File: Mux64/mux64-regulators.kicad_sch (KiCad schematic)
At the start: 23 parts

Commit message: Add files via upload
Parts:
- C1, C2, C3, C4, C7: renamed from C?; footprint (none) -> Capacitor_SMD:C_0805_2012Metric
- C10, C11, C12, C5, C6, C8, C9: renamed from C?; footprint (none) -> Capacitor_SMD:C_0201_0603Metric
- gave numbers to parts that had none: 11

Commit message: Add files via upload
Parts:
- J10, J7, J8, J9: footprint (none) -> Connector_PinSocket_1.00mm:PinSocket_2x10_P1.00mm_Vertical_SMD
- R4, R5, R6, R7: footprint (none) -> Resistor_SMD:R_0603_1608Metric
- TP1: footprint (none) -> TestPoint:TestPoint_Pad_D2.5mm
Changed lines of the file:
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@@
       (effects (font (size 0.75 0.75)))
     )
-    (property "Footprint" "" (id 2) (at 121.92 134.62 0)
+    (property "Footprint" "Resistor_SMD:R_0603_1608Metric" (id 2) (at 121.92 134.62 0)
       (effects (font (size 1.27 1.27)) hide)
     )
@@
     (property "Reference" "J7" (id 0) (at 29.21 34.29 0))
     (property "Value" "Conn_01x20" (id 1) (at 29.21 29.21 0))
-    (property "Footprint" "" (id 2) (at 29.21 55.88 0)
+    (property "Footprint" "Connector_PinSocket_1.00mm:PinSocket_2x10_P1.00mm_Vertical_SMD" (id 2) (at 29.21 55.88 0)
       (effects (font (size 1.27 1.27)) hide)
     )
@@
       (effects (font (size 0.75 0.75)))
     )
-    (property "Footprint" "" (id 2) (at 121.92 116.84 0)
+    (property "Footprint" "Resistor_SMD:R_0603_1608Metric" (id 2) (at 121.92 116.84 0)
       (effects (font (size 1.27 1.27)) hide)
     )
@@
       (effects (font (size 0.75 0.75)))
     )
-    (property "Footprint" "" (id 2) (at 125.73 106.68 0)
+    (property "Footprint" "TestPoint:TestPoint_Pad_D2.5mm" (id 2) (at 125.73 106.68 0)
       (effects (font (size 1.27 1.27)) hide)
     )
@@
     (property "Reference" "J10" (id 0) (at 99.06 34.29 0))
     (property "Value" "Conn_01x20" (id 1) (at 99.06 29.21 0))
-    (property "Footprint" "" (id 2) (at 99.06 55.88 0)
+    (property "Footprint" "Connector_PinSocket_1.00mm:PinSocket_2x10_P1.00mm_Vertical_SMD" (id 2) (at 99.06 55.88 0)
       (effects (font (size 1.27 1.27)) hide)
     )
@@
     (property "Reference" "J8" (id 0) (at 52.07 34.29 0))
     (property "Value" "Conn_01x20" (id 1) (at 52.07 29.21 0))
-    (property "Footprint" "" (id 2) (at 52.07 55.88 0)
+    (property "Footprint" "Connector_PinSocket_1.00mm:PinSocket_2x10_P1.00mm_Vertical_SMD" (id 2) (at 52.07 55.88 0)
       (effects (font (size 1.27 1.27)) hide)
     )
@@
       (effects (font (size 0.75 0.75)))
     )
-    (property "Footprint" "" (id 2) (at 121.92 140.97 0)
+    (property "Footprint" "Resistor_SMD:R_0603_1608Metric" (id 2) (at 121.92 140.97 0)
       (effects (font (size 1.27 1.27)) hide)
     )
@@
     (property "Reference" "J9" (id 0) (at 76.2 34.29 0))
     (property "Value" "Conn_01x20" (id 1) (at 76.2 29.21 0))
-    (property "Footprint" "" (id 2) (at 76.2 55.88 0)
+    (property "Footprint" "Connector_PinSocket_1.00mm:PinSocket_2x10_P1.00mm_Vertical_SMD" (id 2) (at 76.2 55.88 0)
       (effects (font (size 1.27 1.27)) hide)
     )
@@
       (effects (font (size 0.75 0.75)))
     )
-    (property "Footprint" "" (id 2) (at 129.54 116.84 0)
-      (effects (font (size 1.27 1.27)) hide)
-    )
+    (property "Footprint" "Resistor_SMD:R_0603_1608Metric" (id 2) (at 129.54 116.84 0)
+      (effects (font (size 1.27 1.27)) hide)
+    )

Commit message: Add files via upload
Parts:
- removed J10, J7, J8, J9: Conn_01x20, Connector_PinSocket_1.00mm:PinSocket_2x10_P1.00mm_Vertical_SMD, symbol Connector_Generic:Conn_01x20
- added J10, J7, J8, J9: Conn_01x24, Connector_PinSocket_2.54mm:PinSocket_2x12_P2.54mm_Vertical, symbol Connector_Generic:Conn_01x24
- added R8: 0ohm, Resistor_SMD:R_0805_2012Metric, symbol Device:R_Small_US
- C10, C11, C12, C5, C6, C8, C9: footprint Capacitor_SMD:C_0201_0603Metric -> Capacitor_SMD:C_0805_2012Metric
- R4, R5, R6, R7: footprint Resistor_SMD:R_0603_1608Metric -> Resistor_SMD:R_0805_2012Metric
- U1: footprint (none) -> Package_TO_SOT_SMD:SOT-223-3_TabPin2
- U2: footprint (none) -> Package_TO_SOT_SMD:SOT-23-6
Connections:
- net 1.2V: now also C10.1, C11.1, C12.1, C7.1, C9.1, J10.3 (Pin_3), J10.5 (Pin_5), J10.6 (Pin_6), J10.7 (Pin_7), J10.8 (Pin_8); no longer C10.2, C11.2, C12.2, C7.2, C9.2
- net B_a0(MUX_OUT): now also J10.14 (Pin_14)
- net B_a4: now also J10.13 (Pin_13)
- net B_d0: now also J7.8 (Pin_8)
- net B_d1: now also J7.5 (Pin_5)
- net B_d2: now also J7.6 (Pin_6)
- net B_d3: now also J7.3 (Pin_3)
- net B_d4: now also J7.4 (Pin_4)
- net B_d5: now also J7.2 (Pin_2)
- net GND: now also C10.2, C11.2, C12.2, C7.2, C9.2, J10.1 (Pin_1), J10.10 (Pin_10), J10.11 (Pin_11), J10.12 (Pin_12), J10.2 (Pin_2), J10.9 (Pin_9), J7.23 (Pin_23), J7.24 (Pin_24), J8.23 (Pin_23), J8.24 (Pin_24), J9.23 (Pin_23), J9.24 (Pin_24), R8.1; no longer C10.1, C11.1, C12.1, C7.1, C9.1
- net MUX64_A0: now also J10.15 (Pin_15), J10.16 (Pin_16), J10.17 (Pin_17), J7.10 (Pin_10), J7.7 (Pin_7), J8.15 (Pin_15), J8.2 (Pin_2), J9.11 (Pin_11), J9.13 (Pin_13), J9.15 (Pin_15), J9.17 (Pin_17), J9.19 (Pin_19), J9.2 (Pin_2), J9.3 (Pin_3), J9.9 (Pin_9), R8.2
- net MUX64_A10: now also J7.17 (Pin_17)
- net MUX64_A11: now also J7.20 (Pin_20)
- net MUX64_A12: now also J7.19 (Pin_19)
- net MUX64_A13: now also J7.22 (Pin_22)
- net MUX64_A15: now also J8.4 (Pin_4)
- net MUX64_A16: now also J8.3 (Pin_3)
- net MUX64_A17: now also J8.6 (Pin_6)
- net MUX64_A18: now also J8.5 (Pin_5)
- net MUX64_A19: now also J8.8 (Pin_8)
- net MUX64_A2: now also J7.9 (Pin_9)
- net MUX64_A20: now also J8.7 (Pin_7)
- net MUX64_A21: now also J8.10 (Pin_10)
- net MUX64_A22: now also J8.9 (Pin_9)
- net MUX64_A23: now also J8.12 (Pin_12)
- net MUX64_A24: now also J8.11 (Pin_11)
- net MUX64_A25: now also J8.14 (Pin_14)
- net MUX64_A26: now also J8.13 (Pin_13)
- net MUX64_A27: now also J8.16 (Pin_16)
- net MUX64_A29: now also J8.18 (Pin_18)
- net MUX64_A3: now also J7.12 (Pin_12)
- net MUX64_A30: now also J8.17 (Pin_17)
- net MUX64_A31: now also J8.20 (Pin_20)
- net MUX64_A32: now also J8.19 (Pin_19)
- net MUX64_A33: now also J8.22 (Pin_22)
- net MUX64_A35: now also J9.4 (Pin_4)
- net MUX64_A37: now also J9.6 (Pin_6)
- net MUX64_A38: now also J9.5 (Pin_5)
- net MUX64_A39: now also J9.8 (Pin_8)
- net MUX64_A4: now also J7.11 (Pin_11)
- net MUX64_A40: now also J9.7 (Pin_7)
- net MUX64_A41: now also J9.10 (Pin_10)
- net MUX64_A43: now also J9.12 (Pin_12)
- net MUX64_A45: now also J9.14 (Pin_14)
- net MUX64_A47: now also J9.16 (Pin_16)
- net MUX64_A49: now also J9.18 (Pin_18)
- net MUX64_A5: now also J7.14 (Pin_14)
- net MUX64_A51: now also J9.20 (Pin_20)
- net MUX64_A53: now also J9.22 (Pin_22)
- net MUX64_A54: now also J10.23 (Pin_23)
- net MUX64_A55: now also J10.21 (Pin_21)
- net MUX64_A56: now also J10.22 (Pin_22)
- net MUX64_A57: now also J10.19 (Pin_19)
- net MUX64_A58: now also J10.20 (Pin_20)
- net MUX64_A6: now also J7.13 (Pin_13)
- net MUX64_A60: now also J10.18 (Pin_18)
- net MUX64_A7: now also J7.16 (Pin_16)
- net MUX64_A8: now also J7.15 (Pin_15)
- net MUX64_A9: now also J7.18 (Pin_18)
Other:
- note added: "Unused Mux inputs"

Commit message: Add files via upload
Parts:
- removed R8: 0ohm, Resistor_SMD:R_0805_2012Metric, symbol Device:R_Small_US
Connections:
- net MUX64_A0 is gone; now on net GND: J10.15 (Pin_15), J10.16 (Pin_16), J10.17 (Pin_17), J7.10 (Pin_10), J7.7 (Pin_7), J8.15 (Pin_15), J8.2 (Pin_2), J9.11 (Pin_11), J9.13 (Pin_13), J9.15 (Pin_15), J9.17 (Pin_17), J9.19 (Pin_19), J9.2 (Pin_2), J9.3 (Pin_3), J9.9 (Pin_9)
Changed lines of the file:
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@@
     (stroke (width 0) (type default) (color 0 0 0 0))
   )
-  (wire (pts (xy 182.88 35.56) (xy 182.88 109.22))
+  (wire (pts (xy 182.88 30.48) (xy 182.88 109.22))
     (stroke (width 0) (type default) (color 0 0 0 0))
   )
@@
     (pin "1")
   )
-  (symbol (lib_id "Device:R_Small_US") (at 182.88 33.02 0) (unit 1)
-    (in_bom yes) (on_board yes)
-    (property "Reference" "R8" (id 0) (at 182.88 33.02 90)
-      (effects (font (size 0.25 0.25)))
-    )
-    (property "Value" "0ohm" (id 1) (at 184.15 33.02 90)
-      (effects (font (size 0.75 0.75)))
-    )
-    (property "Footprint" "Resistor_SMD:R_0805_2012Metric" (id 2) (at 182.88 33.02 0)
-      (effects (font (size 1.27 1.27)) hide)
-    )
-    (property "Datasheet" "~" (id 3) (at 182.88 33.02 0)
-      (effects (font (size 1.27 1.27)) hide)
-    )
-    (pin "1")
-    (pin "2")
-  )
   (symbol (lib_id "Device:C_Small") (at 138.43 53.34 0) (unit 1)

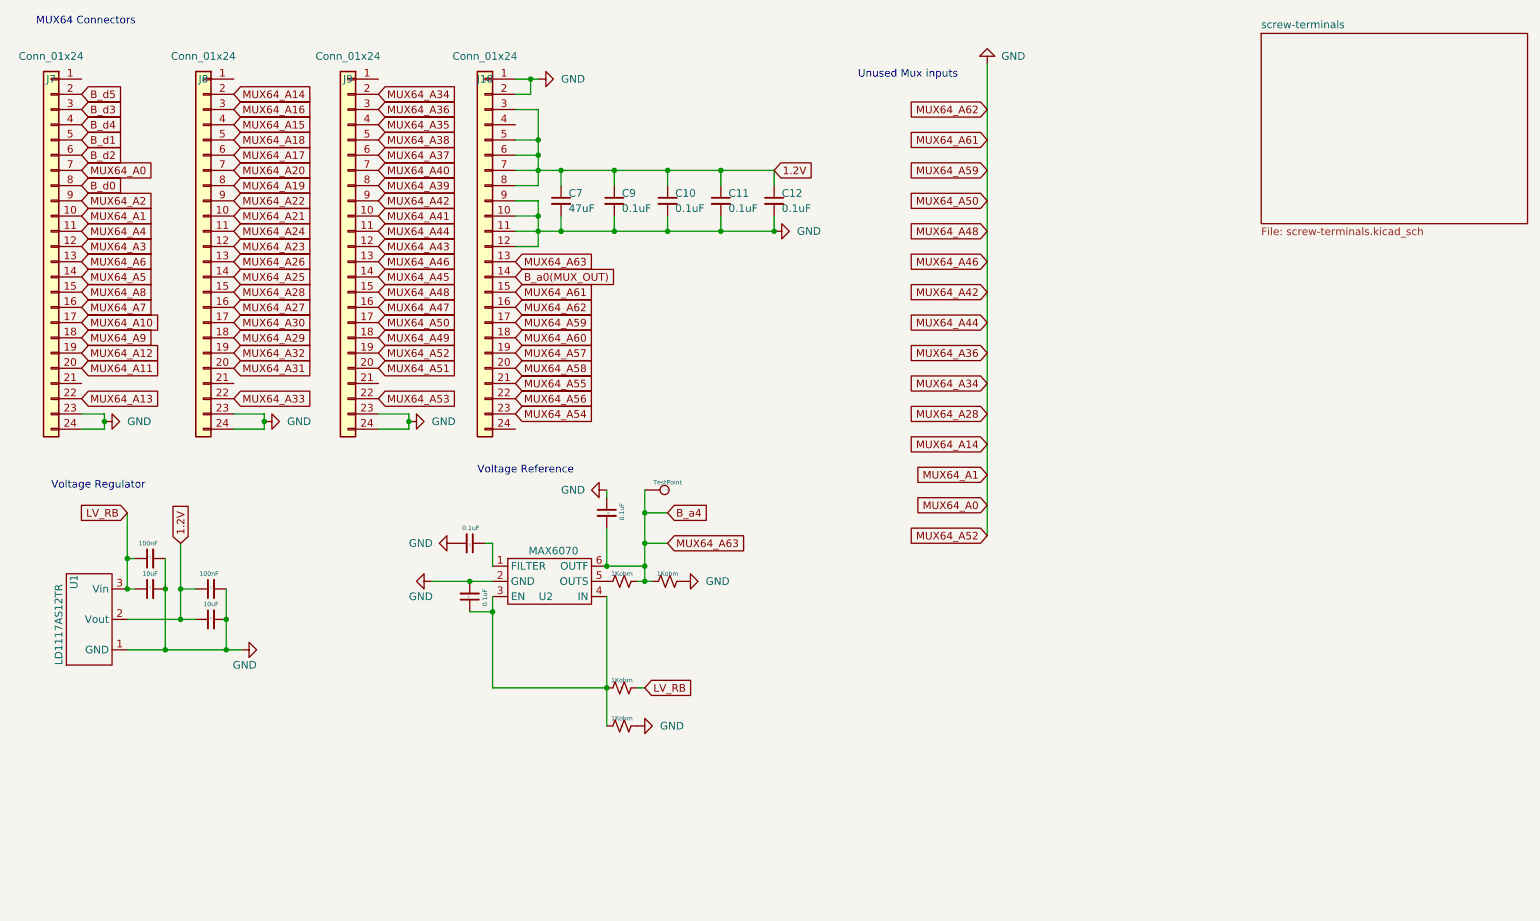
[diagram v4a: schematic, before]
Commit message: Final revision
Fixed high voltage spacial issue and distributed traces to have less density on the bottom of the board
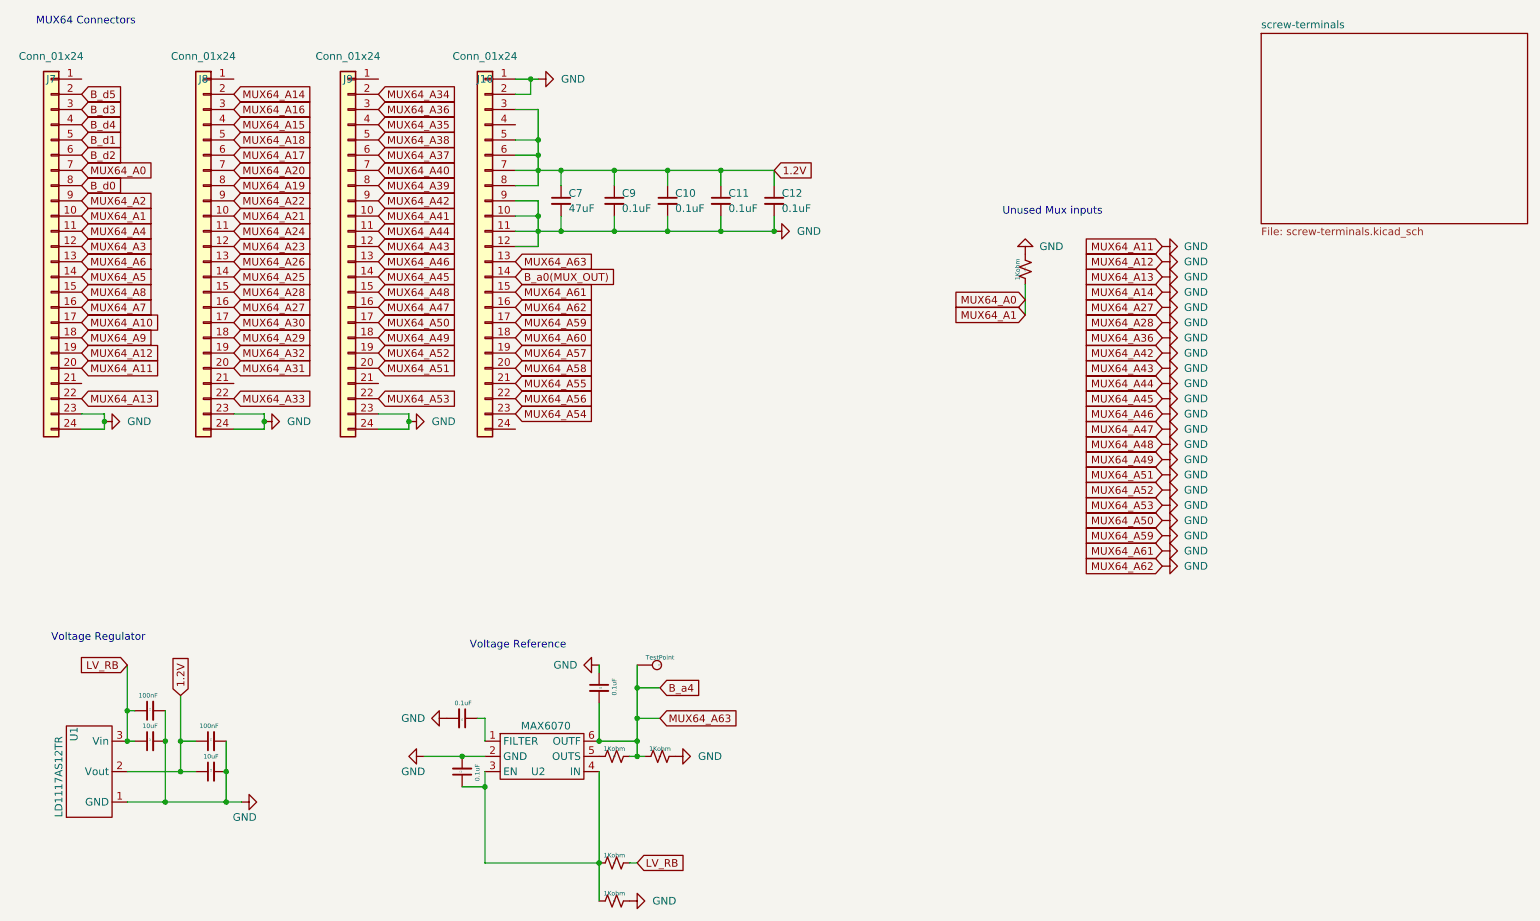
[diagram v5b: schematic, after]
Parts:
- added R23: 1Kohm, Resistor_SMD:R_0805_2012Metric, symbol Device:R_Small_US
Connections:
- net MUX64_A11 is gone; now on net GND: J7.20 (Pin_20)
- net MUX64_A12 is gone; now on net GND: J7.19 (Pin_19)
- net MUX64_A13 is gone; now on net GND: J7.22 (Pin_22)
- net MUX64_A27 is gone; now on net GND: J8.16 (Pin_16)
- net MUX64_A43 is gone; now on net GND: J9.12 (Pin_12)
- net MUX64_A45 is gone; now on net GND: J9.14 (Pin_14)
- net MUX64_A47 is gone; now on net GND: J9.16 (Pin_16)
- net MUX64_A49 is gone; now on net GND: J9.18 (Pin_18)
- net MUX64_A51 is gone; now on net GND: J9.20 (Pin_20)
- net MUX64_A53 is gone; now on net GND: J9.22 (Pin_22)
- net GND: now also R23.2; no longer J7.10 (Pin_10), J7.7 (Pin_7), J9.2 (Pin_2)
- new net MUX64_A0: J7.10 (Pin_10), J7.7 (Pin_7), R23.1
- new net MUX64_A34: J9.2 (Pin_2)
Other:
- moved on the sheet: C1, C2, C3, C4, C5, C6, C8, R4, R5, R6, R7, TP1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
